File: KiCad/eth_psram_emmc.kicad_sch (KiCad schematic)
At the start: 42 parts, among them IC6 IS21EF04GP-JQLI, IC7 LAN8742A-CZ-TR, IC8 APS256XXN-OBR-BG, Y2 VXM7-9032-25M0000000

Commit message: #13
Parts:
- renumbered R9 to R10, R10 to R11, R11 to R12, R12 to R5, R5 to R6, R6 to R7, R7 to R8, R8 to R9
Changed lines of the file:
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@@
 	(title_block
 		(title "${project_name}")
-		(date "2026-01-17")
+		(date "2026-01-29")
 		(rev "${project_version}")
 		(company "${project_creator}")
@@
 	)
 	(junction
+		(at 63.5 81.28)
+		(diameter 0)
+		(color 0 0 0 0)
+	)
+	(junction
 		(at 99.06 170.18)
 		(diameter 0)
@@
 	)
 	(junction
-		(at 63.5 81.28)
-		(diameter 0)
-		(color 0 0 0 0)
-	)
-	(junction
 		(at 99.06 160.02)
 		(diameter 0)
@@
 	(wire
 		(pts
+			(xy 63.5 81.28) (xy 78.74 81.28)
+		)
+		(stroke
+			(width 0)
+			(type default)
+		)
+	)
+	(wire
+		(pts
 			(xy 167.64 66.04) (xy 167.64 73.66)
 		)
@@
 	(wire
 		(pts
-			(xy 175.26 78.74) (xy 177.8 78.74)
-		)
-		(stroke
-			(width 0.1524)
-			(type solid)
-		)
-	)
-	(wire
-		(pts
 			(xy 50.8 76.2) (xy 50.8 81.28)
 		)
@@
 	(wire
 		(pts
-			(xy 63.5 81.28) (xy 78.74 81.28)
-		)
-		(stroke
-			(width 0)
-			(type default)
-		)
-	)
-	(wire
-		(pts
 			(xy 96.52 134.62) (xy 99.06 134.62)
 		)
@@
 		(on_board yes)
 		(dnp no)
-		(property "Reference" "R10"
+		(property "Reference" "R11"
 			(at 136.525 48.26 90)
 			(effects
@@
 			(project "BB3plus CM5 STM32H7 module"
 				(path "/1a4f0aea-3a69-423f-8790-3103cd0321c4/db533ab3-e8cc-4dba-934e-bd27ee1dfc29"
-					(reference "R10")
+					(reference "R11")
 					(unit 1)
 				)
@@
 		(on_board yes)
 		(dnp no)
-		(property "Reference" "#SUPPLY027"
+		(property "Reference" "#SUPPLY028"
 			(at 134.62 86.36 0)
 			(effects
@@
 			(project "BB3plus CM5 STM32H7 module"
 				(path "/1a4f0aea-3a69-423f-8790-3103cd0321c4/db533ab3-e8cc-4dba-934e-bd27ee1dfc29"
-					(reference "#SUPPLY027")
+					(reference "#SUPPLY028")
 					(unit 1)
 				)
@@
 		(on_board yes)
 		(dnp no)
-		(property "Reference" "R6"
+		(property "Reference" "R7"
 			(at 67.945 28.575 90)
 			(effects
@@
 			(project "BB3plus CM5 STM32H7 module"
 				(path "/1a4f0aea-3a69-423f-8790-3103cd0321c4/db533ab3-e8cc-4dba-934e-bd27ee1dfc29"
-					(reference "R6")
+					(reference "R7")
 					(unit 1)
 				)
@@
 		(on_board yes)
 		(dnp no)
-		(property "Reference" "#SUPPLY031"
+		(property "Reference" "#SUPPLY032"
 			(at 185.42 50.8 0)
 			(effects
@@
 			(project "BB3plus CM5 STM32H7 module"
 				(path "/1a4f0aea-3a69-423f-8790-3103cd0321c4/db533ab3-e8cc-4dba-934e-bd27ee1dfc29"
-					(reference "#SUPPLY031")
+					(reference "#SUPPLY032")
 					(unit 1)
 				)
@@
 		(on_board yes)
 		(dnp no)
-		(property "Reference" "#SUPPLY049"
+		(property "Reference" "#SUPPLY021"
 			(at 48.26 50.8 0)
 			(effects
@@
 			(project "BB3plus CM5 STM32H7 module"
 				(path "/1a4f0aea-3a69-423f-8790-3103cd0321c4/db533ab3-e8cc-4dba-934e-bd27ee1dfc29"
-					(reference "#SUPPLY049")
+					(reference "#SUPPLY021")
 					(unit 1)
 				)
@@
 		(on_board yes)
 		(dnp no)
-		(property "Reference" "#SUPPLY029"
+		(property "Reference" "#SUPPLY030"
 			(at 142.24 50.8 0)
 			(effects
@@
 			(project "BB3plus CM5 STM32H7 module"
 				(path "/1a4f0aea-3a69-423f-8790-3103cd0321c4/db533ab3-e8cc-4dba-934e-bd27ee1dfc29"
-					(reference "#SUPPLY029")
+					(reference "#SUPPLY030")
 					(unit 1)
 				)
@@
 		(on_board yes)
 		(dnp no)
-		(property "Reference" "#SUPPLY024"
+		(property "Reference" "#SUPPLY025"
 			(at 109.22 109.22 0)
 			(effects
@@
 			(project "BB3plus CM5 STM32H7 module"
 				(path "/1a4f0aea-3a69-423f-8790-3103cd0321c4/db533ab3-e8cc-4dba-934e-bd27ee1dfc29"
-					(reference "#SUPPLY024")
+					(reference "#SUPPLY025")
 					(unit 1)
 				)
@@
 		(on_board yes)
 		(dnp no)
-		(property "Reference" "#SUPPLY032"
+		(property "Reference" "#SUPPLY033"
 			(at 233.68 162.56 0)
 			(effects
@@
 			(project "BB3plus CM5 STM32H7 module"
 				(path "/1a4f0aea-3a69-423f-8790-3103cd0321c4/db533ab3-e8cc-4dba-934e-bd27ee1dfc29"
-					(reference "#SUPPLY032")
+					(reference "#SUPPLY033")
 					(unit 1)
 				)
@@
 		(on_board yes)
 		(dnp no)
-		(property "Reference" "#SUPPLY023"
+		(property "Reference" "#SUPPLY024"
 			(at 99.06 172.72 0)
 			(effects
@@
 			(project "BB3plus CM5 STM32H7 module"
 				(path "/1a4f0aea-3a69-423f-8790-3103cd0321c4/db533ab3-e8cc-4dba-934e-bd27ee1dfc29"
-					(reference "#SUPPLY023")
+					(reference "#SUPPLY024")
 					(unit 1)
 				)
@@
 		(on_board yes)
 		(dnp no)
-		(property "Reference" "R7"
+		(property "Reference" "R8"
 			(at 70.485 28.575 90)
 			(effects
@@
 			(project "BB3plus CM5 STM32H7 module"
 				(path "/1a4f0aea-3a69-423f-8790-3103cd0321c4/db533ab3-e8cc-4dba-934e-bd27ee1dfc29"
-					(reference "R7")
+					(reference "R8")
 					(unit 1)
 				)
@@
 		(on_board yes)
 		(dnp no)
-		(property "Reference" "#SUPPLY033"
+		(property "Reference" "#SUPPLY034"
 			(at 256.54 152.4 0)
 			(effects
@@
 			(project "BB3plus CM5 STM32H7 module"
 				(path "/1a4f0aea-3a69-423f-8790-3103cd0321c4/db533ab3-e8cc-4dba-934e-bd27ee1dfc29"
-					(reference "#SUPPLY033")
+					(reference "#SUPPLY034")
 					(unit 1)
 				)
@@
 		(on_board yes)
 		(dnp no)
-		(property "Reference" "#SUPPLY022"
+		(property "Reference" "#SUPPLY023"
 			(at 63.5 175.26 0)
 			(effects
@@
 			(project "BB3plus CM5 STM32H7 module"
 				(path "/1a4f0aea-3a69-423f-8790-3103cd0321c4/db533ab3-e8cc-4dba-934e-bd27ee1dfc29"
-					(reference "#SUPPLY022")
+					(reference "#SUPPLY023")
 					(unit 1)
 				)
@@
 		(on_board yes)
 		(dnp no)
-		(property "Reference" "#SUPPLY021"
+		(property "Reference" "#SUPPLY022"
 			(at 48.26 78.74 0)
 			(effects
@@
 			(project "BB3plus CM5 STM32H7 module"
 				(path "/1a4f0aea-3a69-423f-8790-3103cd0321c4/db533ab3-e8cc-4dba-934e-bd27ee1dfc29"
-					(reference "#SUPPLY021")
+					(reference "#SUPPLY022")
 					(unit 1)
 				)
@@
 		(on_board yes)
 		(dnp no)
-		(property "Reference" "R11"
+		(property "Reference" "R12"
 			(at 173.99 70.485 0)
 			(effects
@@
 			(project "BB3plus CM5 STM32H7 module"
 				(path "/1a4f0aea-3a69-423f-8790-3103cd0321c4/db533ab3-e8cc-4dba-934e-bd27ee1dfc29"
-					(reference "R11")
+					(reference "R12")
 					(unit 1)
 				)
@@
 		(on_board yes)
 		(dnp no)
-		(property "Reference" "R5"
+		(property "Reference" "R6"
 			(at 62.23 22.86 0)
 			(effects
@@
 			(project "BB3plus CM5 STM32H7 module"
 				(path "/1a4f0aea-3a69-423f-8790-3103cd0321c4/db533ab3-e8cc-4dba-934e-bd27ee1dfc29"
-					(reference "R5")
+					(reference "R6")
 					(unit 1)
 				)
@@
 	(symbol
 		(lib_id "power:GND")
-		(at 177.8 78.74 0)
+		(at 175.26 78.74 0)
 		(mirror y)
 		(unit 1)
@@
 		(on_board yes)
 		(dnp no)
-		(property "Reference" "#SUPPLY030"
-			(at 177.8 78.74 0)
+		(property "Reference" "#SUPPLY031"
+			(at 175.26 78.74 0)
 			(effects
 				(font
@@
 		)
 		(property "Value" "GND"
-			(at 179.705 80.01 0)
+			(at 177.165 80.01 0)
 			(effects
 				(font
@@
 		)
 		(property "Footprint" ""
-			(at 177.8 78.74 0)
+			(at 175.26 78.74 0)
 			(effects
 				(font
@@
 		)
 		(property "Datasheet" ""
-			(at 177.8 78.74 0)
+			(at 175.26 78.74 0)
 			(effects
 				(font
@@
 		)
 		(property "Description" "Power symbol creates a global label with name \"GND\" , ground"
-			(at 177.8 78.74 0)
+			(at 175.26 78.74 0)
 			(effects
 				(font
@@
 			(project "BB3plus CM5 STM32H7 module"
 				(path "/1a4f0aea-3a69-423f-8790-3103cd0321c4/db533ab3-e8cc-4dba-934e-bd27ee1dfc29"
-					(reference "#SUPPLY030")
+					(reference "#SUPPLY031")
 					(unit 1)
 				)
@@
 		(on_board yes)
 		(dnp no)
-		(property "Reference" "#SUPPLY028"
+		(property "Reference" "#SUPPLY029"
 			(at 139.7 60.96 0)
 			(effects
@@
 			(project "BB3plus CM5 STM32H7 module"
 				(path "/1a4f0aea-3a69-423f-8790-3103cd0321c4/db533ab3-e8cc-4dba-934e-bd27ee1dfc29"
-					(reference "#SUPPLY028")
+					(reference "#SUPPLY029")
 					(unit 1)
 				)
@@
 		(on_board yes)
 		(dnp no)
-		(property "Reference" "#SUPPLY025"
+		(property "Reference" "#SUPPLY026"
 			(at 109.22 132.08 0)
 			(effects
@@
 			(project "BB3plus CM5 STM32H7 module"
 				(path "/1a4f0aea-3a69-423f-8790-3103cd0321c4/db533ab3-e8cc-4dba-934e-bd27ee1dfc29"
-					(reference "#SUPPLY025")
+					(reference "#SUPPLY026")
 					(unit 1)
 				)
@@
 		(on_board yes)
 		(dnp no)
-		(property "Reference" "#SUPPLY026"
+		(property "Reference" "#SUPPLY027"
 			(at 109.22 157.48 0)
 			(effects
@@
 			(project "BB3plus CM5 STM32H7 module"
 				(path "/1a4f0aea-3a69-423f-8790-3103cd0321c4/db533ab3-e8cc-4dba-934e-bd27ee1dfc29"
-					(reference "#SUPPLY026")
+					(reference "#SUPPLY027")
 					(unit 1)
 				)
@@
 		(on_board yes)
 		(dnp yes)
-		(property "Reference" "R12"
+		(property "Reference" "R5"
 			(at 53.34 49.53 90)
 			(effects
@@
 			(project "BB3plus CM5 STM32H7 module"
 				(path "/1a4f0aea-3a69-423f-8790-3103cd0321c4/db533ab3-e8cc-4dba-934e-bd27ee1dfc29"
-					(reference "R12")
+					(reference "R5")
 					(unit 1)
 				)
@@
 		(on_board yes)
 		(dnp no)
-		(property "Reference" "R8"
+		(property "Reference" "R9"
 			(at 73.025 28.575 90)
 			(effects
@@
 			(project "BB3plus CM5 STM32H7 module"
 				(path "/1a4f0aea-3a69-423f-8790-3103cd0321c4/db533ab3-e8cc-4dba-934e-bd27ee1dfc29"
-					(reference "R8")
+					(reference "R9")
 					(unit 1)
 				)
@@
 		(on_board yes)
 		(dnp no)
-		(property "Reference" "R9"
+		(property "Reference" "R10"
 			(at 75.565 28.575 90)
 			(effects
@@
 			(project "BB3plus CM5 STM32H7 module"
 				(path "/1a4f0aea-3a69-423f-8790-3103cd0321c4/db533ab3-e8cc-4dba-934e-bd27ee1dfc29"
-					(reference "R9")
+					(reference "R10")
 					(unit 1)
 				)

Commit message: #14
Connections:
- net +1V8: no longer IC6.M7 (VCCQ)
- net GND: now also IC6.M7 (VCCQ)
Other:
- note added: "Max consumption HS200 mode +3V3 (Vcc): Read 40 mA, Write 40 mA +1V8 (Vccq): Read 140 mA, Write 80 mA"
- note added: "Max consumption Read/Write @250MHz (X8/X16): 32/40 mA"
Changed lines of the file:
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@@
 	(title_block
 		(title "${project_name}")
-		(date "2026-01-29")
+		(date "2026-03-26")
 		(rev "${project_version}")
 		(company "${project_creator}")
@@
 		)
 	)
+	(text "Max consumption Read/Write @250MHz (X8/X16): 32/40 mA"
+		(exclude_from_sim no)
+		(at 228.6 107.315 0)
+		(effects
+			(font
+				(size 0.889 0.889)
+				(color 132 0 132 1)
+			)
+			(justify left bottom)
+		)
+	)
 	(text "PC4"
 		(exclude_from_sim no)
@@
 		)
 	)
+	(text "Max consumption HS200 mode\n+3V3 (Vcc): Read 40 mA, Write 40 mA\n+1V8 (Vccq): Read 140 mA, Write 80 mA"
+		(exclude_from_sim no)
+		(at 71.12 179.07 0)
+		(effects
+			(font
+				(size 0.889 0.889)
+				(color 132 0 132 1)
+			)
+			(justify left top)
+		)
+	)
 	(text "PC5"
 		(exclude_from_sim no)
@@
 	)
 	(junction
+		(at 99.06 172.72)
+		(diameter 0)
+		(color 0 0 0 0)
+	)
+	(junction
 		(at 243.84 144.78)
 		(diameter 0)
@@
 	)
 	(junction
-		(at 99.06 142.24)
-		(diameter 0)
-		(color 0 0 0 0)
-	)
-	(junction
 		(at 134.62 71.12)
 		(diameter 0)
@@
 	(wire
 		(pts
-			(xy 96.52 144.78) (xy 99.06 144.78)
-		)
-		(stroke
-			(width 0)
-			(type default)
-		)
-	)
-	(wire
-		(pts
 			(xy 182.88 134.62) (xy 198.12 134.62)
 		)
@@
 	(wire
 		(pts
-			(xy 99.06 142.24) (xy 99.06 144.78)
-		)
-		(stroke
-			(width 0)
-			(type default)
-		)
-	)
-	(wire
-		(pts
 			(xy 60.96 81.28) (xy 63.5 81.28)
 		)
@@
 	(wire
 		(pts
+			(xy 96.52 172.72) (xy 99.06 172.72)
+		)
+		(stroke
+			(width 0)
+			(type default)
+		)
+	)
+	(wire
+		(pts
 			(xy 96.52 106.68) (xy 99.06 106.68)
 		)
@@
 		)
 	)
+	(wire
+		(pts
+			(xy 99.06 172.72) (xy 99.06 175.26)
+		)
+		(stroke
+			(width 0)
+			(type default)
+		)
+	)
 	(bus
 		(pts
@@
 	(symbol
 		(lib_id "power:GND")
-		(at 99.06 172.72 0)
-		(mirror y)
+		(at 99.06 175.26 0)
 		(unit 1)
 		(exclude_from_sim no)
@@
 		(dnp no)
 		(property "Reference" "#SUPPLY024"
-			(at 99.06 172.72 0)
+			(at 99.06 175.26 0)
 			(effects
 				(font
@@
 		)
 		(property "Value" "GND"
-			(at 93.345 173.99 0)
+			(at 104.775 176.53 0)
 			(effects
 				(font
@@
 		)
 		(property "Footprint" ""
-			(at 99.06 172.72 0)
+			(at 99.06 175.26 0)
 			(effects
 				(font
@@
 		)
 		(property "Datasheet" ""
-			(at 99.06 172.72 0)
+			(at 99.06 175.26 0)
 			(effects
 				(font
@@
 		)
 		(property "Description" "Power symbol creates a global label with name \"GND\" , ground"
-			(at 99.06 172.72 0)
+			(at 99.06 175.26 0)
 			(effects
 				(font

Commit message: #16
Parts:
- renumbered C58 to C43, C51 to C44, C43 to C45, C54 to C46, C56 to C47, C52 to C48, C55 to C49, C57 to C50, C53 to C51, C44 to C52, C45 to C53, C48 to C54, C46 to C55, C49 to C56, C59 to C57, C60 to C58, C61 to C59, C62 to C60, C47 to C61, C50 to C62, IC7 to IC6, IC6 to IC7, R16 to R11, R17 to R12, R5 to R13, R11 to R14, R18 to R15, R14 to R16, R19 to R17, R12 to R18, R13 to R19, R15 to R5

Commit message: #18, OSHW ID121
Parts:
- C43, C54, C56, C57, C59, C62: LCSC (none) -> C60474
- C44, C46, C49: LCSC (none) -> C15195
- C45, C52: LCSC (none) -> C76945
- IC6: LCSC (none) -> C621424
- R14: LCSC (none) -> C132157
- RN1, RN2: LCSC (none) -> C840641
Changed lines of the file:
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@@
 	(title_block
 		(title "${project_name}")
-		(date "2026-03-28")
+		(date "2026-04-04")
 		(rev "${project_version}")
 		(company "${project_creator}")
@@
 			)
 		)
-		(property "LCSC" ""
+		(property "LCSC" "C840641"
 			(at 40.64 53.34 0)
 			(effects
@@
 			)
 		)
-		(property "LCSC" ""
+		(property "LCSC" "C15195"
 			(at 149.86 76.2 0)
 			(effects
@@
 			)
 		)
-		(property "LCSC" ""
+		(property "LCSC" "C840641"
 			(at 40.64 43.18 0)
 			(effects
@@
 			)
 		)
-		(property "LCSC" ""
+		(property "LCSC" "C840641"
 			(at 40.64 38.1 0)
 			(effects
@@
 			)
 		)
-		(property "LCSC" ""
+		(property "LCSC" "C132157"
 			(at 134.62 50.8 0)
 			(effects
@@
 			)
 		)
-		(property "LCSC" ""
+		(property "LCSC" "C15195"
 			(at 144.78 71.12 0)
 			(effects
@@
 			)
 		)
-		(property "LCSC" ""
+		(property "LCSC" "C60474"
 			(at 109.22 127 0)
 			(effects
@@
 			)
 		)
-		(property "LCSC" ""
+		(property "LCSC" "C60474"
 			(at 238.76 147.32 0)
 			(effects
@@
 			)
 		)
-		(property "LCSC" ""
+		(property "LCSC" "C60474"
 			(at 185.42 48.26 0)
 			(effects
@@
 			)
 		)
-		(property "LCSC" ""
+		(property "LCSC" "C15195"
 			(at 132.08 58.42 0)
 			(effects
@@
 		)
 		(instances
-			(project ""
+			(project "BB3plus CM5 STM32H7 module"
 				(path "/1a4f0aea-3a69-423f-8790-3103cd0321c4/db533ab3-e8cc-4dba-934e-bd27ee1dfc29"
 					(reference "IC7")
@@
 			)
 		)
-		(property "LCSC" ""
+		(property "LCSC" "C840641"
 			(at 40.64 45.72 0)
 			(effects
@@
 			)
 		)
-		(property "LCSC" ""
+		(property "LCSC" "C840641"
 			(at 40.64 55.88 0)
 			(effects
@@
 			)
 		)
-		(property "LCSC" ""
+		(property "LCSC" "C840641"
 			(at 40.64 66.04 0)
 			(effects
@@
 			)
 		)
-		(property "LCSC" ""
+		(property "LCSC" "C60474"
 			(at 109.22 152.4 0)
 			(effects
@@
 			)
 		)
-		(property "LCSC" ""
+		(property "LCSC" "C60474"
 			(at 109.22 104.14 0)
 			(effects
@@
 			)
 		)
-		(property "Type" ""
+		(property "LCSC" "C621424"
 			(at 104.14 53.34 0)
 			(effects
@@
 			)
 		)
-		(property "LCSC" ""
+		(property "LCSC" "C76945"
 			(at 55.88 71.12 0)
 			(effects
@@
 			)
 		)
-		(property "LCSC" ""
+		(property "LCSC" "C76945"
 			(at 55.88 81.28 0)
 			(effects
@@
 			)
 		)
-		(property "LCSC" ""
+		(property "LCSC" "C840641"
 			(at 40.64 35.56 0)
 			(effects
@@
 			)
 		)
-		(property "LCSC" ""
+		(property "LCSC" "C60474"
 			(at 251.46 147.32 0)
 			(effects
@@
 			)
 		)
-		(property "LCSC" ""
+		(property "LCSC" "C840641"
 			(at 40.64 58.42 0)
 			(effects

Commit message: #19
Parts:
- removed C54, C56, C62: 100n, PCM_EEZ_passives:C_0402_1005Metric, symbol PCM_EEZ_passives:C-EU
- removed C55, C61: 2u2, PCM_EEZ_passives:C_0402_1005Metric, symbol PCM_EEZ_passives:C-EU
- removed IC7: IS21EF04GP-JQLI, PCM_EEZ_BGA:IS21EF04GP-JQLI, symbol PCM_EEZ_ICs:IS21EF04GP-JQLI
- added R20, R21, R22, R23, R24: 47K, PCM_EEZ_passives:R_0402_1005Metric, symbol PCM_EEZ_passives:R-EU
- added X2: 5033981892, PCM_EEZ_connectors:5033981892, symbol PCM_EEZ_connectors:5033981892
- C53: value 2u2 -> 10u; footprint PCM_EEZ_passives:C_0402_1005Metric -> PCM_EEZ_passives:C_0603_1608Metric; DigiKey 490-GRM155C71A225KE11JCT-ND -> 1276-1052-6-ND; LCSC C2211665 -> C17024; Mouser 81-GRM155C71A225KE1J -> 187-CL21A106KPFNNNE; TME - -> CL21A106KPFNNNE
- renumbered C57 to C54, C58 to C55, C59 to C56, C60 to C57, IC8 to IC7
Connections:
- net +3V3: now also C53.2, R20.1, R21.1, R22.1, R23.1, R24.1, X2.4 (VDD); no longer C53.1
- net GND: now also C53.1, X2.6 (VSS), X2.SH, X2.SW2; no longer C53.2
- net SDMMC_CLK: now also X2.5 (CLK)
- net SDMMC_CMD: now also R24.2, X2.3 (CMD)
- net SDMMC_D0: now also R22.2, X2.7 (DAT0)
- net SDMMC_D1: now also R23.2, X2.8 (DAT1)
- net SDMMC_D2: now also R20.2, X2.1 (DAT2)
- net SDMMC_D3: now also R21.2, X2.2 (CD/DAT3)
- new net ~{SD_DETECT}: X2.SW1
- no-connect marks 1 -> 0
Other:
- note added: "Micro SD card socket"
- note removed: "Max consumption HS200 mode +3V3 (Vcc): Read 40 mA, Write 40 mA +1V8 (Vccq): Read 140 mA, Write 80 mA"
- note removed: "eMMC 4 GB"

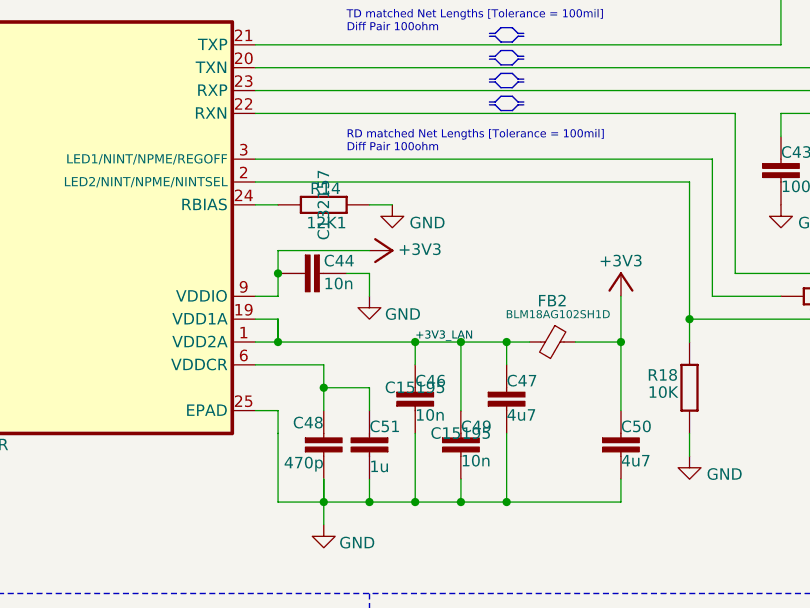
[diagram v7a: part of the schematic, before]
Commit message: USB lanes renamed, OSHWA logo added
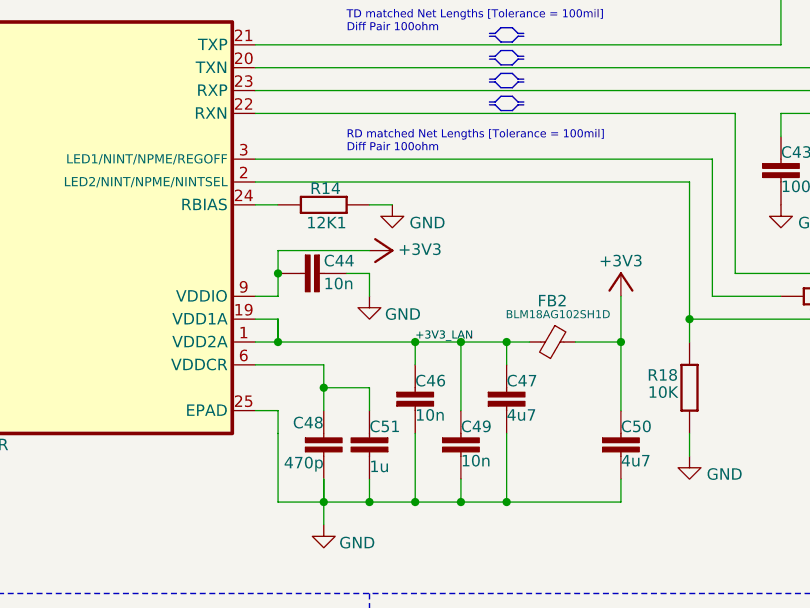
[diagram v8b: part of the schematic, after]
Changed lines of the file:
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@@
 	(title_block
 		(title "${project_name}")
-		(date "2026-04-09")
+		(date "2026-04-18")
 		(rev "${project_version}")
 		(company "${project_creator}")
@@
 		(property "LCSC" "C15195"
 			(at 149.86 76.2 0)
+			(hide yes)
 			(show_name no)
 			(do_not_autoplace no)
@@
 		(property "LCSC" "C132157"
 			(at 134.62 50.8 0)
+			(hide yes)
 			(show_name no)
 			(do_not_autoplace no)
@@
 		(property "LCSC" "C15195"
 			(at 144.78 71.12 0)
+			(hide yes)
 			(show_name no)
 			(do_not_autoplace no)
